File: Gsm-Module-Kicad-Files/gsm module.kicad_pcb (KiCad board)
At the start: 2 copper layers, 108.7 x 76.1 mm, 79 parts, among them J1 SIM_Card, J2 Conn_01x05_Male, J3 USB_OTG, J5 Conn_01x02_Male, J6 8P8C_LED_Shielded, Q1 2N2219, SW1 SW_Push, U2 MG2608, U3 SN65HVD10, U4 MCP1700-1202E_SOT23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

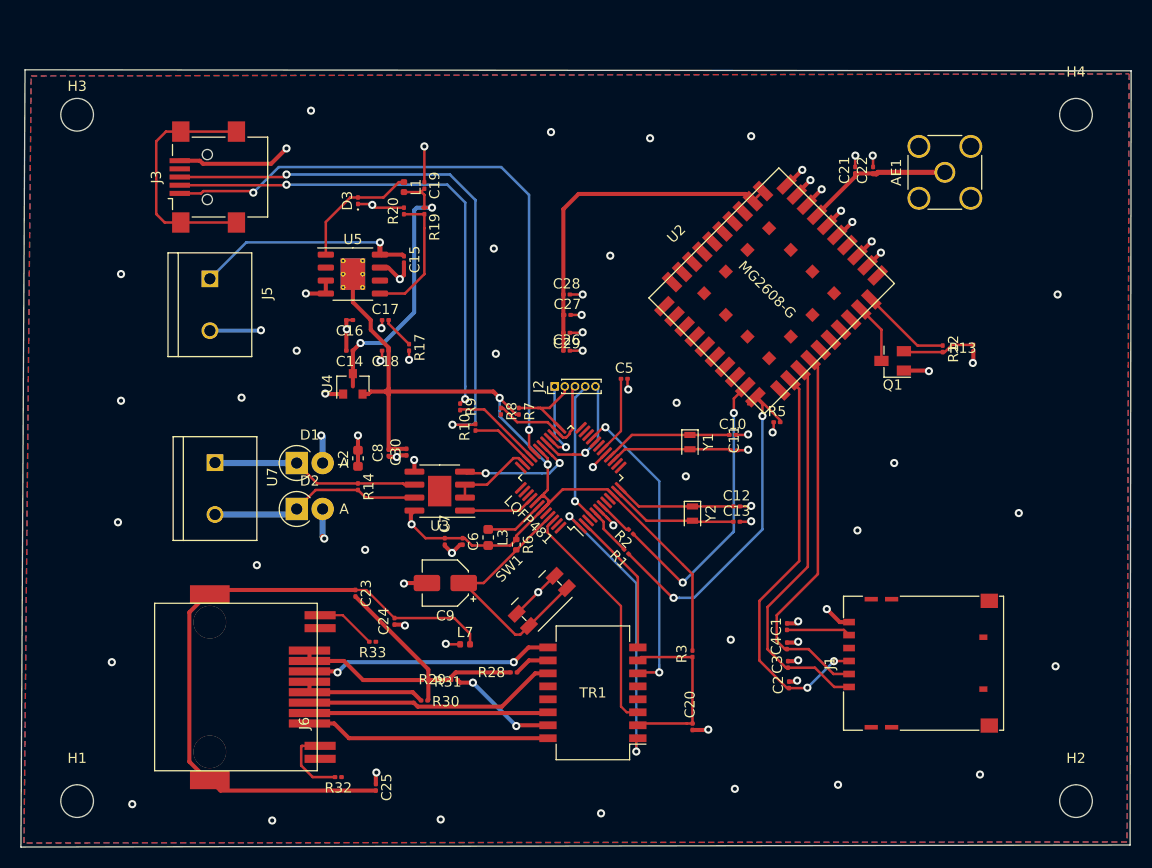
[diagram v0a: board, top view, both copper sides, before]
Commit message: Update gsm module.kicad_pcb
PCB measure edit
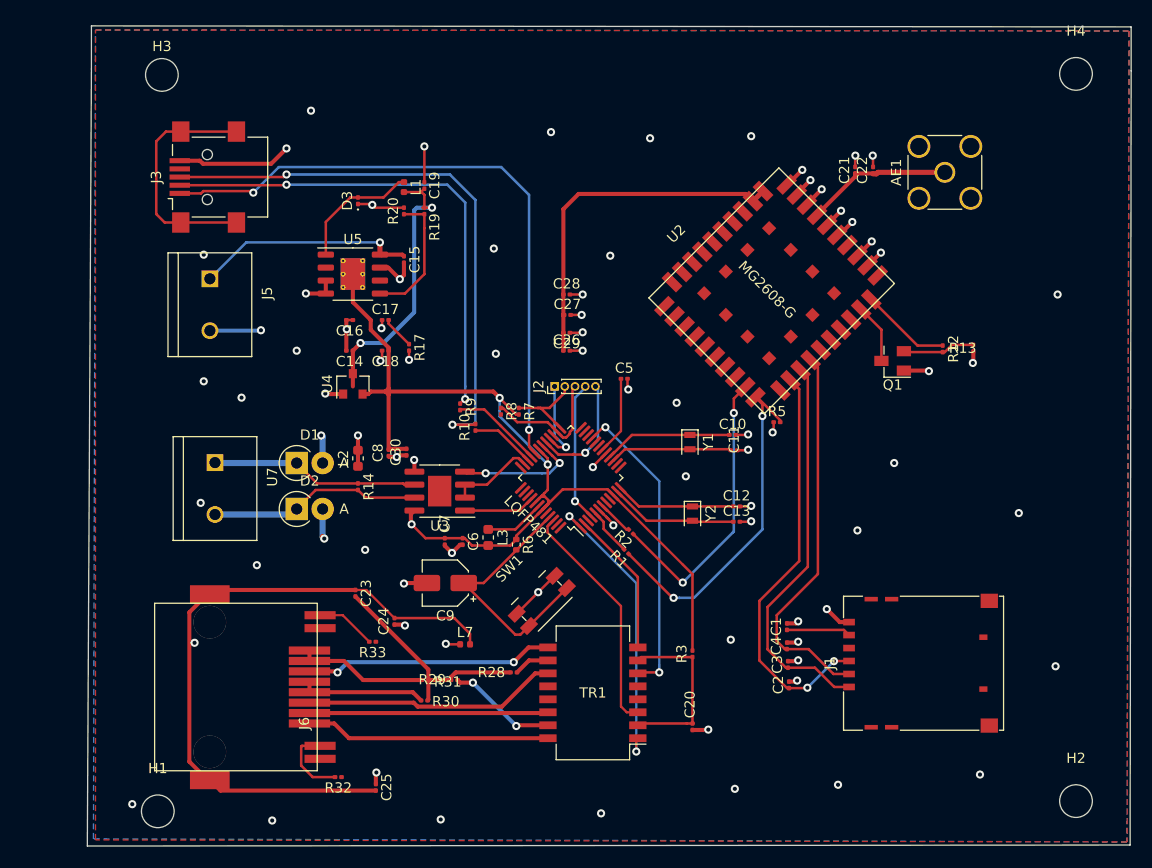
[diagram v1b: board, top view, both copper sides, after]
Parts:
- moved H3 9.17 mm to (85.3, 52.5)
- moved H1 7.96 mm to (84.9, 124.6)
- moved H4 4.00 mm to (174.8, 52.4)
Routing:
- net Net-(R1-Pad1): track 35.5 -> 34.5 mm
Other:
- board size 108.7 x 76.1 mm -> 102.2 x 80.3 mm

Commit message: edited
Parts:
- moved C26 17.3 mm to (131.4, 63.5), turned to 90 degrees
- moved C29 14.9 mm to (128.9, 63.4), turned to 270 degrees
- moved C27 12.8 mm to (127.1, 63.4), turned to 90 degrees
- moved C28 10.6 mm to (124.8, 63.4), turned to 90 degrees
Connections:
- C26 pad 1: 4V1 -> +4V
- C27 pad 1: 4V1 -> +4V
- C28 pad 1: 4V1 -> +4V
- C29 pad 2: 4V1 -> +4V
- U2 pad 31: 4V1 -> +4V
- U2 pad 32: 4V1 -> +4V
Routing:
- net +4V: track 27.7 -> 62.9 mm
- net 4V1: track 34.8 -> 0.00 mm

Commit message: edit
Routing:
- net /ethernet/SHİELD: track 65.2 -> 68.8 mm
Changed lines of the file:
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@@
     (thickness 1.6)
     (drawings 6)
-    (tracks 624)
+    (tracks 626)
     (zones 0)
     (modules 79)
@@
     (tags capacitor)
     (attr smd)
-    (fp_text reference C29 (at 0 -1.05 90) (layer F.SilkS)
+    (fp_text reference C29 (at -0.08 0.85 90) (layer F.SilkS)
       (effects (font (size 1 1) (thickness 0.15)))
     )
@@
   (segment (start 106.65 68.9) (end 106.65 68.9) (width 0.5) (layer F.Cu) (net 11))
   (via (at 106.65 68.9) (size 0.8) (drill 0.4) (layers F.Cu B.Cu) (net 11))
-  (segment (start 93.56 68.9) (end 90 72.46) (width 0.25) (layer B.Cu) (net 11))
-  (segment (start 106.65 68.9) (end 93.56 68.9) (width 0.25) (layer B.Cu) (net 11))
+  (segment (start 93.56 68.9) (end 90 72.46) (width 0.4) (layer B.Cu) (net 11))
+  (segment (start 106.65 68.9) (end 93.56 68.9) (width 0.4) (layer B.Cu) (net 11))
   (segment (start 107.45 70.095) (end 106.65 70.095) (width 0.25) (layer F.Cu) (net 11))
   (segment (start 106.805 70.25) (end 106.65 70.095) (width 0.25) (layer F.Cu) (net 11))
@@
   (segment (start 106.25 122.57) (end 91.0395 122.57) (width 0.4) (layer F.Cu) (net 14))
   (segment (start 89.733798 103.3762) (end 89.99386 103.3762) (width 0.4) (layer F.Cu) (net 14))
-  (segment (start 87.989999 105.119999) (end 89.733798 103.3762) (width 0.4) (layer F.Cu) (net 14))
-  (segment (start 87.989999 119.740001) (end 87.989999 105.119999) (width 0.4) (layer F.Cu) (net 14))
-  (segment (start 89.774498 121.5245) (end 87.989999 119.740001) (width 0.4) (layer F.Cu) (net 14))
   (segment (start 89.994 121.5245) (end 89.774498 121.5245) (width 0.4) (layer F.Cu) (net 14))
   (segment (start 108.07 105.68) (end 113.93 105.68) (width 0.25) (layer F.Cu) (net 14))
   (segment (start 115.47 107.22) (end 115.47 108.25) (width 0.25) (layer F.Cu) (net 14))
   (segment (start 113.93 105.68) (end 115.47 107.22) (width 0.25) (layer F.Cu) (net 14))
+  (segment (start 88.6245 121.5245) (end 89.994 121.5245) (width 0.25) (layer F.Cu) (net 14))
+  (segment (start 86.05 118.95) (end 88.6245 121.5245) (width 0.25) (layer F.Cu) (net 14))
+  (segment (start 86.05 105.65) (end 86.05 118.95) (width 0.25) (layer F.Cu) (net 14))
+  (segment (start 88.3238 103.3762) (end 86.05 105.65) (width 0.25) (layer F.Cu) (net 14))
+  (segment (start 89.99386 103.3762) (end 88.3238 103.3762) (width 0.25) (layer F.Cu) (net 14))
   (segment (start 144.154905 63.871704) (end 143.164955 64.861654) (width 0.5) (layer F.Cu) (net 108))
   (segment (start 143.164955 64.861654) (end 142.457848 64.154547) (width 0.4) (layer F.Cu) (net 108))

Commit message: edited
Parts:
- added R21: 4.7k, Resistor_SMD:R_0201_0603Metric, F.Cu at (106.9, 65.8)
- R20: value 2.33k -> 4.7k
- moved R17 8.41 mm to (101.1, 79.6), turned to 0 degrees
- moved C17 6.08 mm to (101.1, 76.5), turned to 180 degrees
- moved L1 1.35 mm to (107.8, 64.0), turned to 0 degrees
- moved C16 0.63 mm to (103.0, 76.5), turned to 0 degrees
- moved C19 0.41 mm to (111.0, 63.7)
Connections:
- C16 pad 1: GND -> Net-(C16-Pad1)
- C17 pad 1: GND -> Net-(C16-Pad1)
- U5 pad 4: GND -> Net-(C16-Pad1)
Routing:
- net GND: track 109.7 -> 98.7 mm, vias 81 -> 93
- net Net-(C16-Pad1): track 0.00 -> 3.97 mm
- net Net-(D3-Pad2): track 12.5 -> 10.3 mm
- net Net-(R19-Pad2): track 13.0 -> 15.1 mm
- net SIM_CLK: track 38.8 -> 40.2 mm
- net +4V: track 62.9 -> 61.6 mm
- net Net-(R1-Pad1): track 34.5 -> 33.5 mm
- net SIM_DATA: track 38.3 -> 38.9 mm
- net (no net): vias 0 -> 1
